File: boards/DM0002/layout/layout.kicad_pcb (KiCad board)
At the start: 4 copper layers, 15 x 38.6 mm, 59 parts, among them J1 , J2 USB4105-GF-A, SW1 KMR231G LFS, U1 TLV75801PDRV, U2 W25Q16JVUXIQ, U3 SC0914(13), U4 SG-210STF 12.0000ML0

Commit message: Bump stdlib, add auto impedance matching
Signed-off-by: akhilles <akhilvelagapudi@gmail.com>
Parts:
- J1: value (none) -> 1.27mm 5x2

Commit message: Update DM0002 layout
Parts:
- C1: value 1uF 10V -> GRM155Z71A105KE01D
- C10, C11, C12, C13, C16, C17, C3, C4, C5, C6, C7, C8, C9: value 100nF -> GCM155R71H104KE02D
- C14, C15: value 1uF -> GRM155Z71A105KE01D
- C18: value 10uF 10V -> GRM188Z71A106KA73D
- C2: value 4.7uF 10V -> GRM155Z71A105KE01D
- J1: value 1.27mm 5x2 -> 1.27mm 5x2 Vertical
- R1, R10, R11, R12, R13: value 10k -> ERJ-2RKF1002X
- R14, R15: value 27 -> ERJ-2RKF27R0X
- R16: value 33k -> ERJ-2RKF3302X
- R17: value 47k -> ERJ-2RKF4702X
- R18, R19: value 5.1k 5% -> ERJ-2RKF5101X
- R2: value 47k 1% -> ERJ-2RKF4702X
- R3: value 10k 1% -> ERJ-2RKF1002X
- R4: value 110 -> ERJ-2RKF1100X
- R5, R9: value 150 -> ERJ-2RKF1500X
- R6, R7, R8: value 261 -> ERJ-2RKF2610X
- TP2, TP3, TP4, TP5, TP6: value Pad_D1.5mm -> ?

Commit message: Update layout
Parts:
- removed C18: GRM188Z71A106KA73D, C_0603_1608Metric:C_0603_1608Metric
- removed FB1: 220 2A 100MHz, R_0603_1608Metric:R_0603_1608Metric
- D2: value VLMG1500-GS08 -> LTST-C281KGKT-5A
- D3, D4, D5: value VLMO1500-GS08 -> LTST-C281KFKT-5A
- D6: value VLMS1500-GS08 -> LTST-C281KRKT-5A
- D7: value PESD5V0X1UB,135 -> SMF5V0A-E3-08; footprint D_SOD-523:D_SOD-523 -> D_SMF:D_SMF
- J1: value 1.27mm 5x2 Vertical -> 62201021121
- U1: value TLV75801PDRV -> TLV75801PDRVR
- U3: value SC0914(13) -> RP2040
- moved D7 0.97 mm to (136.8, 93.0), turned to 180 degrees
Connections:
- D7 pad 1: USB_C.VBUS_RAW -> VBUS_5V0
- J2 pad A4: USB_C.VBUS_RAW -> VBUS_5V0
- J2 pad A9: USB_C.VBUS_RAW -> VBUS_5V0
- J2 pad B4: USB_C.VBUS_RAW -> VBUS_5V0
- J2 pad B9: USB_C.VBUS_RAW -> VBUS_5V0
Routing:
- net USB_C.VBUS_RAW: track 10.2 -> 0.00 mm
- net VBUS_5V0: track 26.3 -> 35.3 mm
- net GND: track 39.9 -> 40.5 mm, vias 25 -> 24

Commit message: schematics for DM002
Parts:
- D2: value LTST-C281KGKT-5A -> VLMG1500-GS08
- D3, D4, D5: value LTST-C281KFKT-5A -> VLMO1500-GS08
- D6: value LTST-C281KRKT-5A -> VLMS1500-GS08
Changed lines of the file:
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@@
 			)
 		)
-		(property "Value" "LTST-C281KFKT-5A"
+		(property "Value" "VLMO1500-GS08"
 			(at 0 1.17 90)
 			(layer "F.Fab")
@@
 			)
 		)
-		(property "Mpn" "LTST-C281KFKT-5A"
+		(property "Mpn" "VLMO1500-GS08"
 			(at 0 0 0)
 			(layer "F.SilkS")
@@
 			)
 		)
-		(property "Manufacturer" "Lite-On Inc."
+		(property "Manufacturer" "Vishay Semiconductor Opto Division"
+			(at 0 0 0)
+			(layer "F.SilkS")
+			(hide yes)
+			(effects
+				(font
+					(size 1.27 1.27)
+					(thickness 0.15)
+				)
+			)
+		)
+		(property "Alternatives" "{\"mpn\": \"LTST-C281KFKT-5A\", \"manufacturer\": \"Lite-On Inc.\"}"
 			(at 0 0 0)
 			(layer "F.SilkS")
@@
 			)
 		)
-		(property "Value" "LTST-C281KGKT-5A"
+		(property "Value" "VLMG1500-GS08"
 			(at 0 1.17 90)
 			(layer "F.Fab")
@@
 			)
 		)
-		(property "Mpn" "LTST-C281KGKT-5A"
+		(property "Mpn" "VLMG1500-GS08"
 			(at 0 0 0)
 			(layer "F.SilkS")
@@
 			)
 		)
-		(property "Alternatives" "{\"mpn\": \"LTST-C283KGKT-5A\", \"manufacturer\": \"Lite-On Inc.\"}"
+		(property "Alternatives" "{\"mpn\": \"LTST-C281KGKT-5A\", \"manufacturer\": \"Lite-On Inc.\"},{\"mpn\": \"LTST-C283KGKT-5A\", \"manufacturer\": \"Lite-On Inc.\"}"
 			(at 0 0 0)
 			(layer "F.SilkS")
@@
 			)
 		)
-		(property "Manufacturer" "Lite-On Inc."
+		(property "Manufacturer" "Vishay Semiconductor Opto Division"
 			(at 0 0 0)
 			(layer "F.SilkS")
@@
 			)
 		)
-		(property "Value" "LTST-C281KRKT-5A"
+		(property "Value" "VLMS1500-GS08"
 			(at 0 1.17 90)
 			(layer "F.Fab")
@@
 			)
 		)
-		(property "Mpn" "LTST-C281KRKT-5A"
+		(property "Mpn" "VLMS1500-GS08"
 			(at 0 0 0)
 			(layer "F.SilkS")
@@
 			)
 		)
-		(property "Manufacturer" "Lite-On Inc."
+		(property "Manufacturer" "Vishay Semiconductor Opto Division"
 			(at 0 0 0)
 			(layer "F.SilkS")
@@
 			)
 		)
-		(property "Alternatives" "{\"mpn\": \"LTST-C283KRKT-5A\", \"manufacturer\": \"Lite-On Inc.\"}"
+		(property "Alternatives" "{\"mpn\": \"LTST-C281KRKT-5A\", \"manufacturer\": \"Lite-On Inc.\"},{\"mpn\": \"LTST-C283KRKT-5A\", \"manufacturer\": \"Lite-On Inc.\"}"
 			(at 0 0 0)
 			(layer "F.SilkS")
@@
 			)
 		)
-		(property "Value" "LTST-C281KFKT-5A"
+		(property "Value" "VLMO1500-GS08"
 			(at 0 1.17 90)
 			(layer "F.Fab")
@@
 			)
 		)
-		(property "Mpn" "LTST-C281KFKT-5A"
+		(property "Mpn" "VLMO1500-GS08"
 			(at 0 0 0)
 			(layer "F.SilkS")
@@
 			)
 		)
-		(property "Manufacturer" "Lite-On Inc."
+		(property "Manufacturer" "Vishay Semiconductor Opto Division"
+			(at 0 0 0)
+			(layer "F.SilkS")
+			(hide yes)
+			(effects
+				(font
+					(size 1.27 1.27)
+					(thickness 0.15)
+				)
+			)
+		)
+		(property "Alternatives" "{\"mpn\": \"LTST-C281KFKT-5A\", \"manufacturer\": \"Lite-On Inc.\"}"
 			(at 0 0 0)
 			(layer "F.SilkS")
@@
 			)
 		)
-		(attr exclude_from_pos_files exclude_from_bom dnp)
+		(attr exclude_from_pos_files exclude_from_bom)
 		(fp_circle
 			(center 0 0)
@@
 			)
 		)
-		(property "Description" "5–6 V TVS Diode 800–1200 W"
+		(property "Description" "5–6 V TVS Diode"
 			(at 0 0 180)
 			(unlocked yes)
@@
 			)
 		)
-		(property "Alternatives" "{\"mpn\": \"SZSMF5.0AT1G\", \"manufacturer\": \"Vishay General Semiconductor - Diodes Division\"}"
+		(property "Alternatives" "{\"mpn\": \"SZSMF5.0AT1G\", \"manufacturer\": \"Littelfuse Inc.\"}"
 			(at 0 0 0)
 			(layer "F.SilkS")
@@
 			)
 		)
-		(property "Reverse Clamping Voltage" "9–12 V"
+		(property "Reverse Clamping Voltage" "None"
 			(at 0 0 0)
 			(layer "F.SilkS")
@@
 			)
 		)
-		(property "Peak Pulse Power" "800–1200 W"
+		(property "Peak Pulse Power" "None"
 			(at 0 0 0)
 			(layer "F.SilkS")
@@
 			)
 		)
+		(property "Direction" "Unidirectional"
+			(at 0 0 0)
+			(layer "F.SilkS")
+			(hide yes)
+			(effects
+				(font
+					(size 1.27 1.27)
+					(thickness 0.15)
+				)
+			)
+		)
 		(attr smd)
 		(fp_line
@@
 			)
 		)
-		(property "Value" "LTST-C281KFKT-5A"
+		(property "Value" "VLMO1500-GS08"
 			(at 0 1.17 90)
 			(layer "F.Fab")
@@
 			)
 		)
-		(property "Mpn" "LTST-C281KFKT-5A"
+		(property "Mpn" "VLMO1500-GS08"
 			(at 0 0 0)
 			(layer "F.SilkS")
@@
 			)
 		)
-		(property "Manufacturer" "Lite-On Inc."
+		(property "Manufacturer" "Vishay Semiconductor Opto Division"
+			(at 0 0 0)
+			(layer "F.SilkS")
+			(hide yes)
+			(effects
+				(font
+					(size 1.27 1.27)
+					(thickness 0.15)
+				)
+			)
+		)
+		(property "Alternatives" "{\"mpn\": \"LTST-C281KFKT-5A\", \"manufacturer\": \"Lite-On Inc.\"}"
 			(at 0 0 0)
 			(layer "F.SilkS")
@@
 			)
 		)
-		(attr exclude_from_pos_files exclude_from_bom dnp)
+		(attr exclude_from_pos_files exclude_from_bom)
 		(fp_circle
 			(center 0 0)
@@
 			)
 		)
-		(property "Alternatives" "{\"mpn\": \"LTST-C281TBKT-5A\", \"manufacturer\": \"Vishay Semiconductor Opto Division\"},{\"mpn\": \"LTST-C283TBKT-5A\", \"manufacturer\": \"Vishay Semiconductor Opto Division\"}"
+		(property "Alternatives" "{\"mpn\": \"LTST-C281TBKT-5A\", \"manufacturer\": \"Lite-On Inc.\"},{\"mpn\": \"LTST-C283TBKT-5A\", \"manufacturer\": \"Lite-On Inc.\"}"
 			(at 0 0 0)
 			(layer "F.SilkS")
@@
 			)
 		)
-		(attr exclude_from_pos_files exclude_from_bom dnp)
+		(attr exclude_from_pos_files exclude_from_bom)
 		(fp_circle
 			(center 0 0)
@@
 			)
 		)
-		(attr exclude_from_pos_files exclude_from_bom dnp)
+		(attr exclude_from_pos_files exclude_from_bom)
 		(fp_circle
 			(center 0 0)
@@
 			)
 		)
-		(attr exclude_from_pos_files exclude_from_bom dnp)
+		(attr exclude_from_pos_files exclude_from_bom)
 		(fp_circle
 			(center 0 0)

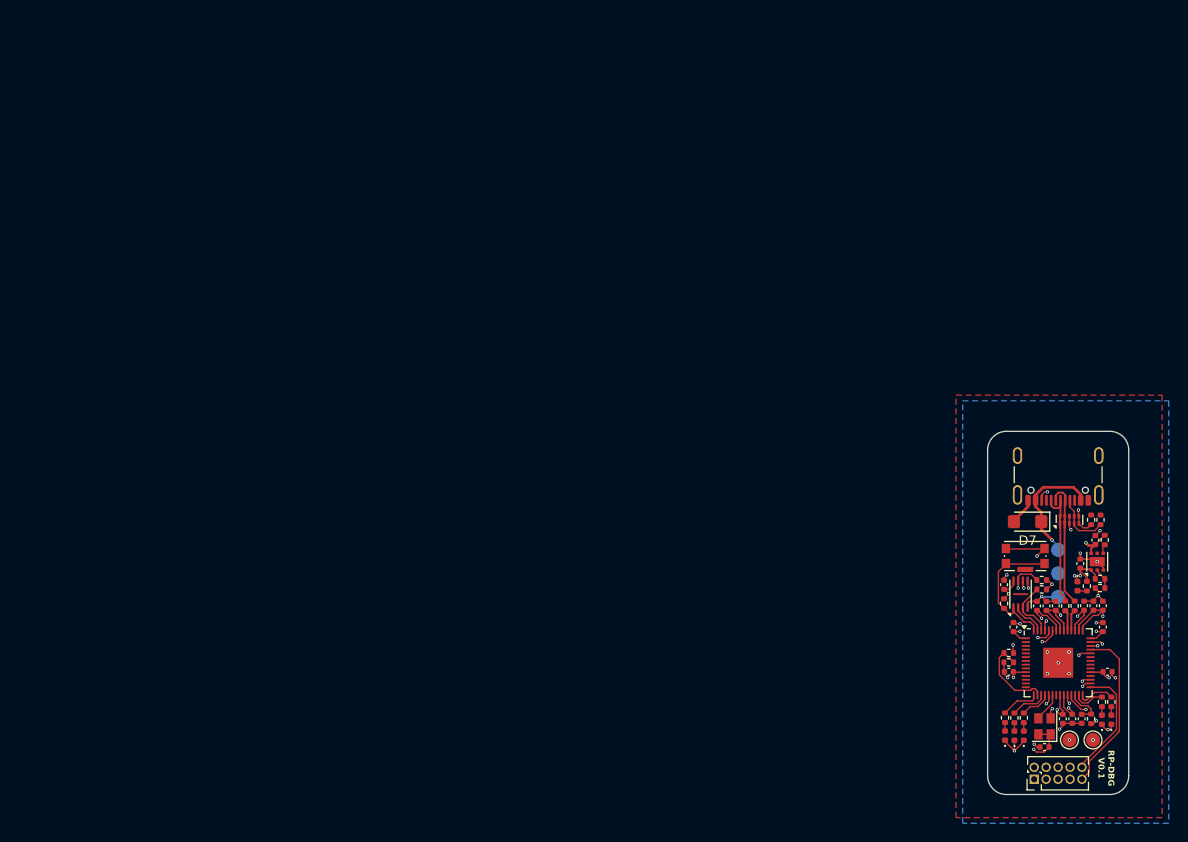
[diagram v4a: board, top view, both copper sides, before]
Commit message: pass drc no unconnected nets + bom matched
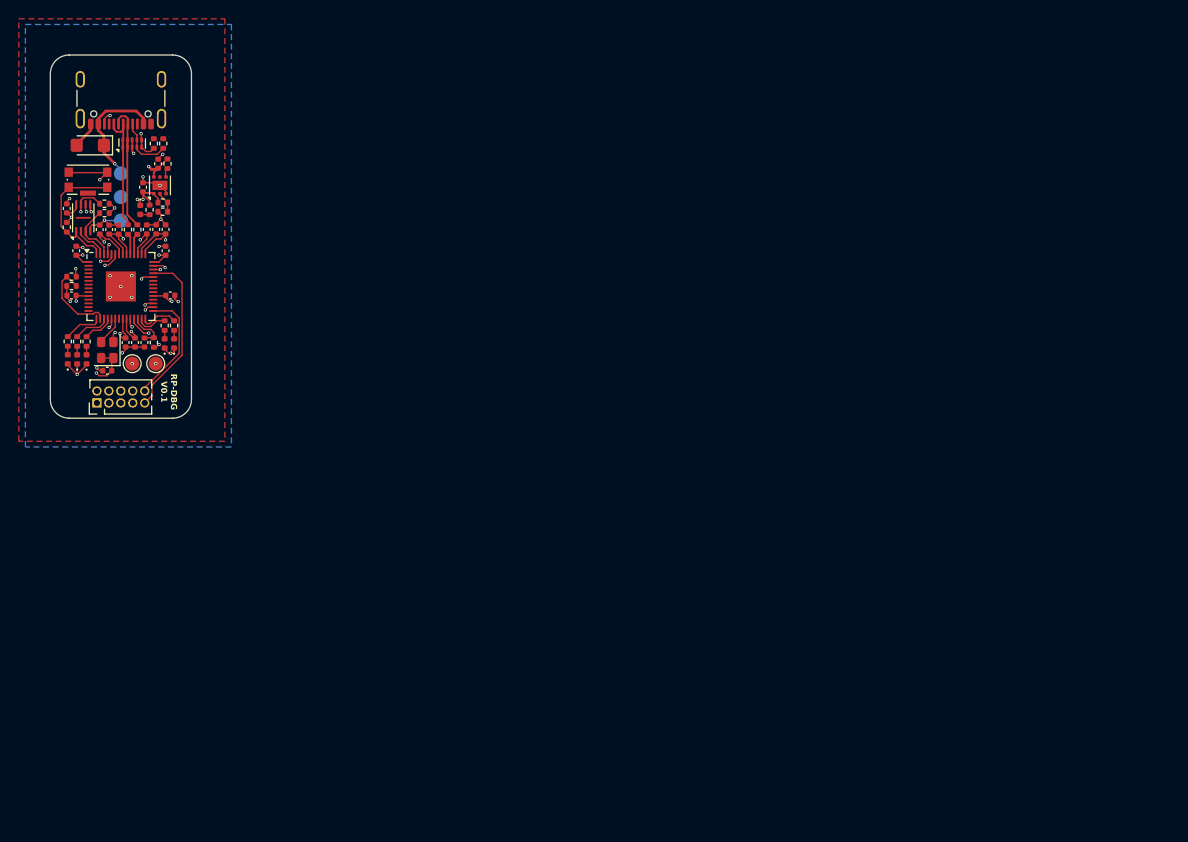
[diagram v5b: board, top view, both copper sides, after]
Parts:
- moved C17 107.3 mm to (38.9, 77.0)
- moved D1 107.3 mm to (46.0, 74.1)
- moved D2 107.3 mm to (45.0, 74.1)
- moved D6 107.3 mm to (42.4, 59.9)
- moved R4 107.3 mm to (46.0, 72.2)
- moved R5 107.3 mm to (45.0, 72.2)
- moved R9 107.3 mm to (43.4, 59.9)
- moved TP1 107.3 mm to (35.3, 79.3)
- moved U1 107.3 mm to (44.5, 57.3)
- moved U4 107.3 mm to (38.9, 74.8)
- moved C10 107.3 mm to (35.1, 69.0)
- moved C11 107.3 mm to (39.1, 62.0)
- moved C12 107.3 mm to (42.9, 74.0)
- moved C13 107.3 mm to (40.1, 62.0)
- moved C14 107.3 mm to (44.1, 61.9)
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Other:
- board text added: "0"
- board text added: "0 mm"
- board text added: "0.01 mm"
- board text added: "0.0152 mm"
- board text added: "0.025"
- board text added: "0.035 mm"
- board text added: "0.0900 mm / 0.0900 mm"
- board text added: "0.1500 mm"
- board text added: "0.2104 mm"
- board text added: "1"
- board text added: "1.065 mm"
- board text added: "1.1412 mm"
- board text added: "15.0000 mm x 38.6000 mm"
- board text added: "3.3"
- board text added: "4"
- board text added: "4.4"
- board text added: "4.6"
- board text added: "B.Cu"
- board text added: "B.Mask"
- board text added: "B.Paste"
- board text added: "B.Silkscreen"
- board text added: "BOARD CHARACTERISTICS"
- board text added: "Black"
- board text added: "Board Thickness:"
- board text added: "Board overall dimensions:"
- board text added: "Bottom Silk Screen"
- board text added: "Bottom Solder Mask"
- board text added: "Bottom Solder Paste"
- board text added: "Castellated pads:"
- board text added: "Color"
- board text added: "Copper Finish:"
- board text added: "Copper Layer Count:"
- board text added: "Dielectric"
- board text added: "ENIG"
- board text added: "Edge card connectors:"
- board text added: "Epsilon R"
- board text added: "F.Cu"
- board text added: "F.Mask"
- board text added: "F.Paste"
- board text added: "F.Silkscreen"
- board text added: "FR4-Core"
- board text added: "Impedance Control:"
- board text added: "In1.Cu"
- board text added: "In2.Cu"
- board text added: "Layer Name"
- board text added: "Loss Tangent"
- board text added: "Material"
- board text added: "Min hole diameter:"
- board text added: "Min track/spacing:"
- board text added: "No"
- board text added: "Not specified"
- board text added: "Plated Board Edge:"
- board text added: "Prepreg"
- board text added: "Thickness (mm)"
- board text added: "Top Silk Screen"
- board text added: "Top Solder Mask"
- board text added: "Top Solder Paste"
- board text added: "Type"
- board text added: "White"
- board text added: "copper"
- board text added: "core"
- board text added: "prepreg"
